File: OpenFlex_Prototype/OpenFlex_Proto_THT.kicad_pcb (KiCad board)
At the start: 2 copper layers, 107.8 x 69.9 mm, 43 parts, among them J2 Molex MAX150_2x10, M3 MountingHole_3.2mm_M3_DIN965_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, Q1 STP80NF55-08, Q2 STP80NF55-08, Q3 STP80NF55-08, Q4 STP80NF55-08, U1 ESP32-S2-DEVKITC-1, U2 LM324, U3 TC4424, U4 TC4424, U5 LM2940S-5.0

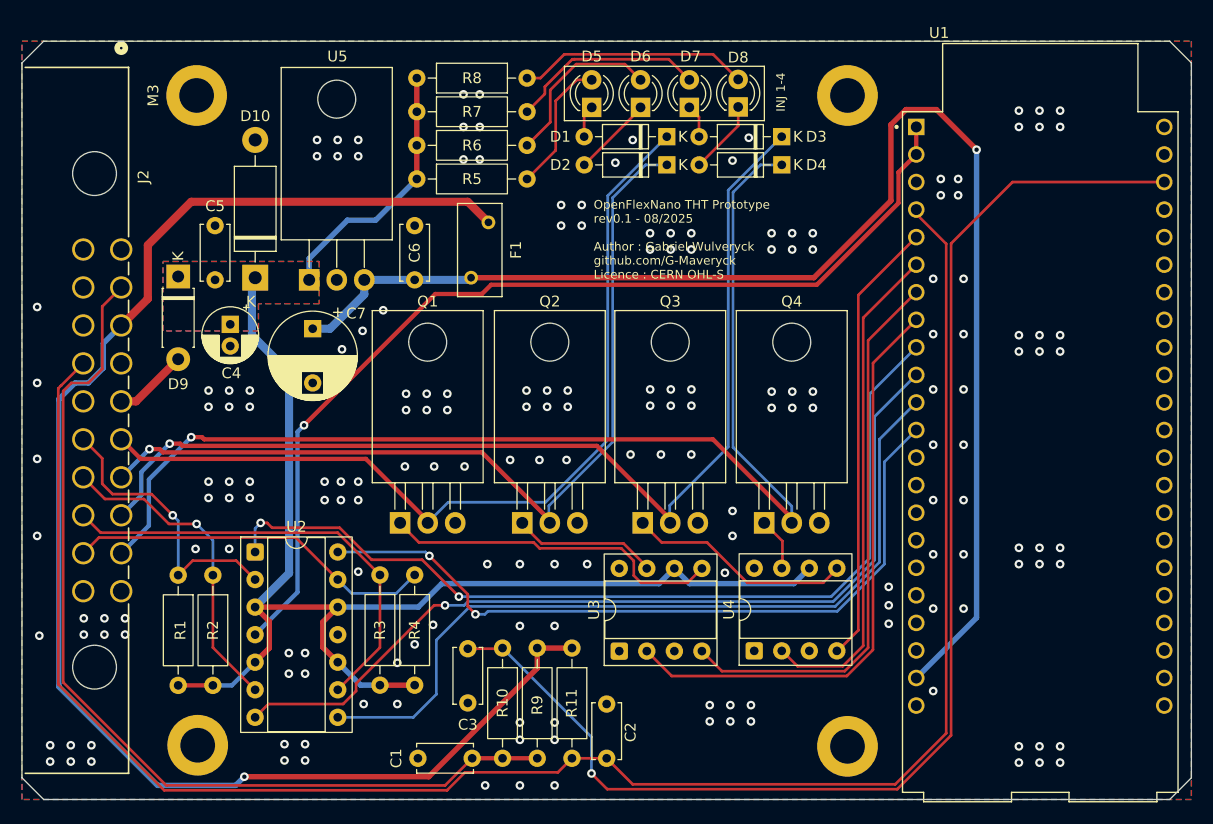
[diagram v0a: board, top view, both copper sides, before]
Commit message: BOM Updated with thermistor. Enclosure in progress
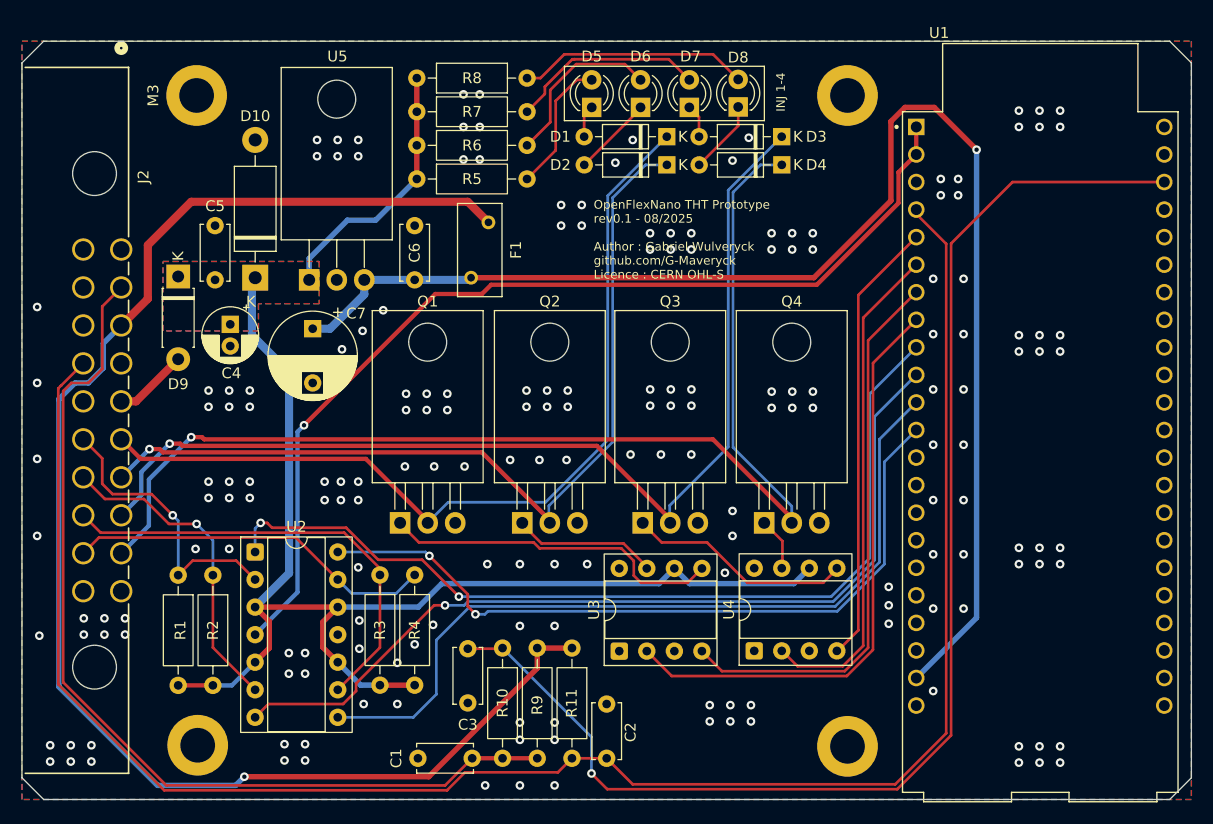
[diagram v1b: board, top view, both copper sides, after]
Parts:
- D9: value SB230TA -> SB230-E3/54
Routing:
- net GND: vias 187 -> 189
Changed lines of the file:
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@@
 			)
 		)
-		(property "Value" "SB230TA"
+		(property "Value" "SB230-E3/54"
 			(at 5.87 -2.5 90)
 			(layer "F.Fab")
@@
 			)
 		)
-		(property "Datasheet" "https://www.mouser.com/datasheet/2/115/ds13002-60388.pdf"
+		(property "Datasheet" "https://www.vishay.com/doc?88717"
 			(at 0 0 270)
 			(unlocked yes)
@@
 			)
 		)
-		(property "Manufacturer_Name" "SMC"
+		(property "Manufacturer_Name" "Vishay Semiconductors"
 			(at 0 0 270)
 			(unlocked yes)
@@
 			)
 		)
-		(property "Manufacturer_Part_Number" "SB230TA"
+		(property "Manufacturer_Part_Number" "SB230-E3/54"
 			(at 0 0 270)
 			(unlocked yes)
@@
 			)
 		)
-		(property "Mouser_Part_Number" "833-SB230-TP "
+		(property "Mouser_Part_Number" "625-SB230-E3"
 			(at 0 0 270)
 			(unlocked yes)
@@
 			)
 		)
-		(property "Mouser URL" "https://www.mouser.fr/ProductDetail/Micro-Commercial-Components-MCC/SB230-TP?qs=P1JMDcb91o64q2VtM2oH0Q%3D%3D"
+		(property "Mouser URL" "https://www.mouser.fr/ProductDetail/Vishay-Semiconductors/SB230-E3-54?qs=u91jd7aysvMVfxBBDX1%252BYQ%3D%3D"
 			(at 0 0 270)
 			(unlocked yes)
@@
 			)
 		)
-		(property "Manufacturer_Name" "ON Semi"
+		(property "Manufacturer_Name" "Texas Instruments"
 			(at 0 0 0)
 			(unlocked yes)
@@
 			)
 		)
-		(property "Manufacturer_Part_Number" "NCV7805BTG"
+		(property "Manufacturer_Part_Number" "LM2940T-5.0/LF08"
 			(at 0 0 0)
 			(unlocked yes)
@@
 			)
 		)
-		(property "URL" "https://www.mouser.fr/ProductDetail/onsemi/NCV7805BTG?qs=8sOby8ZxZLE6UfUj5jjWgw%3D%3D"
+		(property "URL" "https://www.mouser.fr/ProductDetail/Texas-Instruments/LM2940T-5.0-LF08?qs=X1J7HmVL2ZHslyM5jzTq7g%3D%3D"
 			(at 0 0 0)
 			(unlocked yes)
@@
 			)
 		)
-		(property "Mouser_Part_Number" "863-NCV7805BTG"
+		(property "Mouser_Part_Number" "926-LM2940T-50/LF08"
 			(at 0 0 0)
 			(unlocked yes)
@@
 			)
 		)
-		(property "Manufacturer_Name" "Yageo"
+		(property "Manufacturer_Name" "Stackpole Electronics Inc"
 			(at 0 0 90)
 			(unlocked yes)
@@
 			)
 		)
-		(property "Manufacturer_Part_Number" "MFR-25FBF52-2K49"
+		(property "Manufacturer_Part_Number" "RNF14BTE2K49"
 			(at 0 0 90)
 			(unlocked yes)
@@
 			)
 		)
-		(property "URL" "https://www.mouser.fr/ProductDetail/YAGEO/MFR-25FBF52-2K49?qs=oAGoVhmvjhwfmQMP0IrT5Q%3D%3D"
+		(property "URL" "https://www.digikey.fr/fr/products/detail/stackpole-electronics-inc/RNF14BTE2K49/1752591"
+			(at 0 0 90)
+			(unlocked yes)
+			(layer "F.Fab")
+			(hide yes)
+			(effects
+				(font
+					(size 1 1)
+					(thickness 0.15)
+				)
+			)
+		)
+		(property "Mouser_Part_Number" ""
+			(at 0 0 90)
+			(unlocked yes)
+			(layer "F.Fab")
+			(hide yes)
+			(effects
+				(font
+					(size 1 1)
+					(thickness 0.15)
+				)
+			)
+		)
+		(property "Digikey_Part_Number" "738-RNF14BTE2K49CT-ND"
 			(at 0 0 90)
 			(unlocked yes)
@@
 			)
 		)
-		(property "Mouser_Part_Number" "603-MFR-25FBF52-2K49"
+		(property "URL_Mouser" ""
+			(at 0 0 90)
+			(unlocked yes)
+			(layer "F.Fab")
+			(hide yes)
+			(effects
+				(font
+					(size 1 1)
+					(thickness 0.15)
+				)
+			)
+		)
+		(property "URL_Digikey" "https://www.digikey.fr/fr/products/detail/stackpole-electronics-inc/RNF14BTE2K49/1752591"
 			(at 0 0 90)
 			(unlocked yes)
@@
 	)
 	(via
+		(at 179.7 98.7)
+		(size 0.8)
+		(drill 0.4)
+		(layers "F.Cu" "B.Cu")
+		(free yes)
+		(net "GND")
+	)
+	(via
 		(at 177.7 54.4)
 		(size 0.8)
@@
 	)
 	(via
-		(at 179.6 94.2)
+		(at 179.6 93.8)
 		(size 0.8)
 		(drill 0.4)
@@
 	)
 	(via
+		(at 179.7 101.3)
+		(size 0.8)
+		(drill 0.4)
+		(layers "F.Cu" "B.Cu")
+		(free yes)
+		(net "GND")
+	)
+	(via
 		(at 165.8 77.5)
 		(size 0.8)
@@
 	)
 	(segment
+		(start 181.6 93.9)
+		(end 181.6 94.5)
+		(width 0.25)
+		(layer "F.Cu")
+		(net "/Connector/INJ_CH3")
+	)
+	(segment
 		(start 181.6 94.5)
 		(end 181.6 101.195)
@@
 	)
 	(segment
-		(start 177.7 90.6)
-		(end 181.6 94.5)
+		(start 155.850002 90.6)
+		(end 178.3 90.6)
 		(width 0.25)
 		(layer "F.Cu")
@@
 	)
 	(segment
-		(start 155.850002 90.6)
-		(end 177.7 90.6)
+		(start 178.3 90.6)
+		(end 181.6 93.9)
 		(width 0.25)
 		(layer "F.Cu")
@@
 	)
 	(segment
-		(start 232.9 51.6)
-		(end 230.1 51.6)
+		(start 230 51.4)
+		(end 228.7 52.7)
 		(width 0.5)
 		(layer "F.Cu")
@@
 	)
 	(segment
-		(start 230.1 51.6)
-		(end 228.7 53)
+		(start 236.6 55.3)
+		(end 232.7 51.4)
 		(width 0.5)
 		(layer "F.Cu")
@@
 	)
 	(segment
-		(start 228.7 60)
-		(end 221.6 67.1)
+		(start 232.7 51.4)
+		(end 230 51.4)
 		(width 0.5)
 		(layer "F.Cu")
@@
 	)
 	(segment
-		(start 228.7 53)
-		(end 228.7 60)
+		(start 221.6 67.1)
+		(end 190 67.1)
 		(width 0.5)
 		(layer "F.Cu")
@@
 	)
 	(segment
-		(start 236.6 55.3)
-		(end 232.9 51.6)
+		(start 228.7 52.7)
+		(end 228.7 60)
 		(width 0.5)
 		(layer "F.Cu")
@@
 	)
 	(segment
-		(start 221.6 67.1)
-		(end 190 67.1)
+		(start 228.7 60)
+		(end 221.6 67.1)
 		(width 0.5)
 		(layer "F.Cu")
@@
 	)
 	(segment
-		(start 177.886396 90.15)
-		(end 180.836396 93.1)
+		(start 188.875 96.487347)
+		(end 188.875 96.5)
 		(width 0.25)
 		(layer "F.Cu")
@@
 	)
 	(segment
-		(start 170.6 89.7)
-		(end 171.2 89.7)
+		(start 185.487653 93.1)
+		(end 188.875 96.487347)
 		(width 0.25)
 		(layer "F.Cu")
@@
 	)
 	(segment
-		(start 180.836396 93.1)
+		(start 181.436396 93.1)
 		(end 185.487653 93.1)
 		(width 0.25)
@@
 	)
 	(segment
-		(start 171.65 90.15)
-		(end 177.886396 90.15)
+		(start 170.6 89.7)
+		(end 171.2 89.7)
 		(width 0.25)
 		(layer "F.Cu")
@@
 	)
 	(segment
-		(start 188.875 96.487347)
-		(end 188.875 96.5)
+		(start 178.486396 90.15)
+		(end 181.436396 93.1)
 		(width 0.25)
 		(layer "F.Cu")
@@
 	)
 	(segment
-		(start 185.487653 93.1)
-		(end 188.875 96.487347)
+		(start 171.65 90.15)
+		(end 178.486396 90.15)
 		(width 0.25)
 		(layer "F.Cu")
@@
 		(fill yes
 			(thermal_gap 0.5)
-			(thermal_bridge_width 0.5)
+			(thermal_bridge_width 0.65)
 			(smoothing chamfer)
 			(radius 1)
